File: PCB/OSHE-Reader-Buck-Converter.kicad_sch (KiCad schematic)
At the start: 18 parts, among them U3 TPS5432DDA

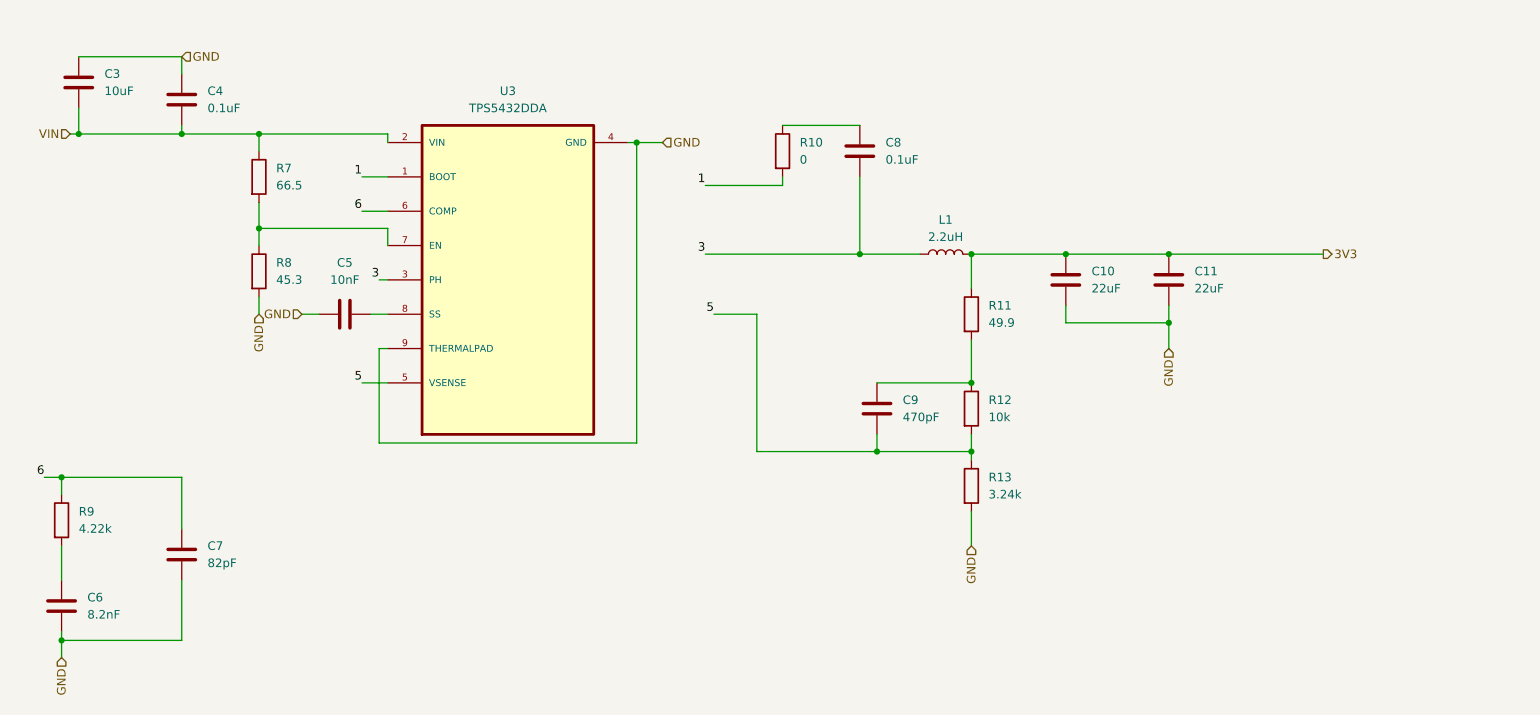
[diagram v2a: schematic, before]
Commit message: Footprints added
All footprints added (problem with J1 for some reason) ((pads of the display driver))
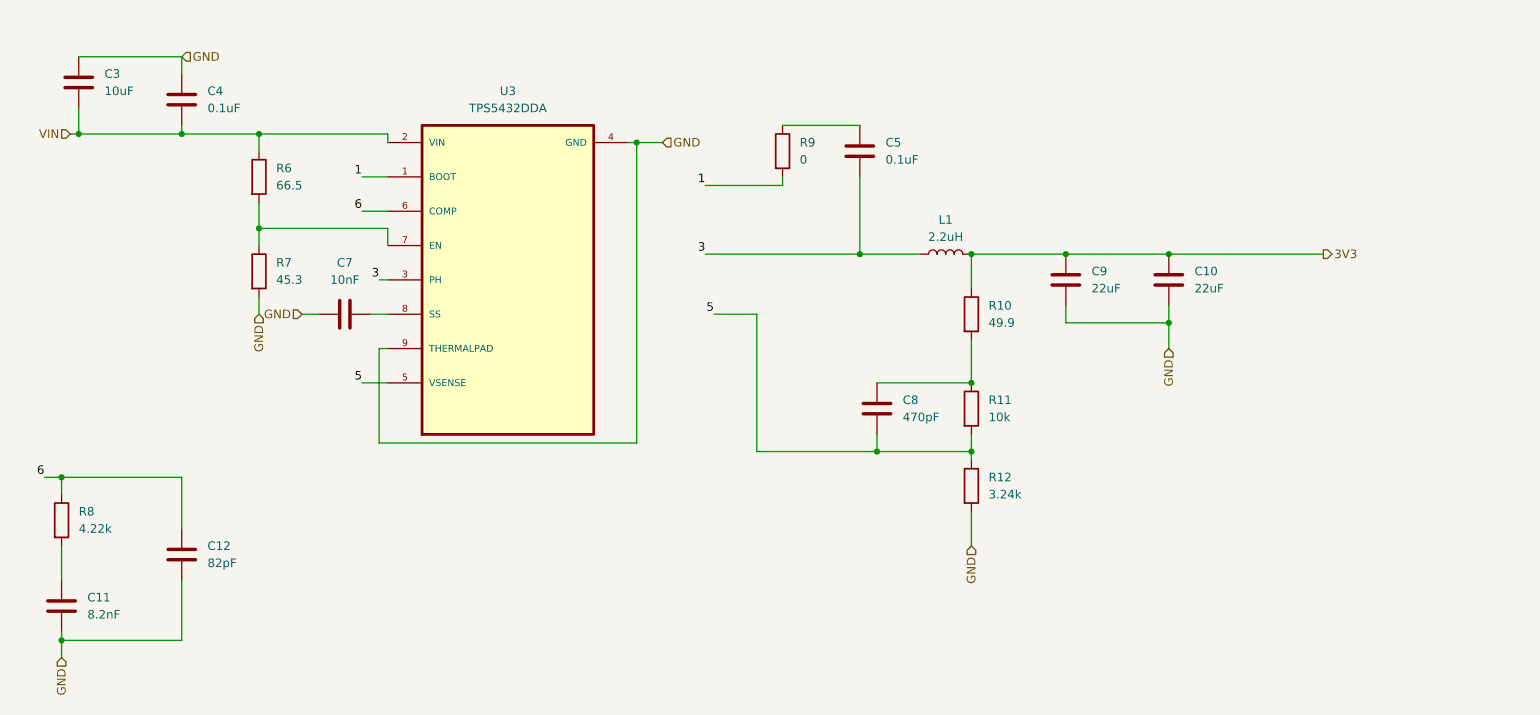
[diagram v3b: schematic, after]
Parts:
- C10: renamed from C11; footprint (none) -> Capacitor_SMD:C_1206_3216Metric
- C11: renamed from C6; footprint (none) -> Capacitor_SMD:C_1206_3216Metric
- C12: renamed from C7; footprint (none) -> Capacitor_SMD:C_1206_3216Metric
- C3, C4: footprint (none) -> Capacitor_SMD:C_1206_3216Metric
- C5: renamed from C8; footprint (none) -> Capacitor_SMD:C_1206_3216Metric
- C7: renamed from C5; footprint (none) -> Capacitor_SMD:C_1206_3216Metric
- C8: renamed from C9; footprint (none) -> Capacitor_SMD:C_1206_3216Metric
- C9: renamed from C10; footprint (none) -> Capacitor_SMD:C_1206_3216Metric
- L1: footprint (none) -> Inductor_SMD:L_1206_3216Metric
- R10: renamed from R11; footprint (none) -> Resistor_SMD:R_1206_3216Metric
- R11: renamed from R12; footprint (none) -> Resistor_SMD:R_1206_3216Metric
- R12: renamed from R13; footprint (none) -> Resistor_SMD:R_1206_3216Metric
- R6: renamed from R7; footprint (none) -> Resistor_SMD:R_1206_3216Metric
- R7: renamed from R8; footprint (none) -> Resistor_SMD:R_1206_3216Metric
- R8: renamed from R9; footprint (none) -> Resistor_SMD:R_1206_3216Metric
- R9: renamed from R10; footprint (none) -> Resistor_SMD:R_1206_3216Metric
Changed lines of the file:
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@@
 		(dnp no)
 		(fields_autoplaced yes)
-		(property "Reference" "R9"
+		(property "Reference" "R8"
 			(at 31.75 82.5499 0)
 			(effects
@@
 			)
 		)
-		(property "Footprint" ""
+		(property "Footprint" "Resistor_SMD:R_1206_3216Metric"
 			(at 27.432 83.82 90)
 			(effects
@@
 				)
 			)
+			(project "OSHE-Reader-Buck-Converter"
+				(path "/d789ce52-9213-4e29-8b23-52a67eafd209"
+					(reference "R8")
+					(unit 1)
+				)
+			)
 		)
 	)
@@
 		(dnp no)
 		(fields_autoplaced yes)
-		(property "Reference" "C11"
+		(property "Reference" "C10"
 			(at 196.85 46.9899 0)
 			(effects
@@
 			)
 		)
-		(property "Footprint" ""
+		(property "Footprint" "Capacitor_SMD:C_1206_3216Metric"
 			(at 192.0748 44.45 0)
 			(effects
@@
 				)
 			)
+			(project "OSHE-Reader-Buck-Converter"
+				(path "/d789ce52-9213-4e29-8b23-52a67eafd209"
+					(reference "C10")
+					(unit 1)
+				)
+			)
 		)
 	)
@@
 		(dnp no)
 		(fields_autoplaced yes)
-		(property "Reference" "C10"
+		(property "Reference" "C9"
 			(at 181.61 46.9899 0)
 			(effects
@@
 			)
 		)
-		(property "Footprint" ""
+		(property "Footprint" "Capacitor_SMD:C_1206_3216Metric"
 			(at 176.8348 44.45 0)
 			(effects
@@
 				)
 			)
+			(project "OSHE-Reader-Buck-Converter"
+				(path "/d789ce52-9213-4e29-8b23-52a67eafd209"
+					(reference "C9")
+					(unit 1)
+				)
+			)
 		)
 	)
@@
 		(dnp no)
 		(fields_autoplaced yes)
-		(property "Reference" "R10"
+		(property "Reference" "R9"
 			(at 138.43 27.9399 0)
 			(effects
@@
 			)
 		)
-		(property "Footprint" ""
+		(property "Footprint" "Resistor_SMD:R_1206_3216Metric"
 			(at 134.112 29.21 90)
 			(effects
@@
 				)
 			)
+			(project "OSHE-Reader-Buck-Converter"
+				(path "/d789ce52-9213-4e29-8b23-52a67eafd209"
+					(reference "R9")
+					(unit 1)
+				)
+			)
 		)
 	)
@@
 		(dnp no)
 		(fields_autoplaced yes)
-		(property "Reference" "C7"
+		(property "Reference" "C12"
 			(at 50.8 87.6299 0)
 			(effects
@@
 			)
 		)
-		(property "Footprint" ""
+		(property "Footprint" "Capacitor_SMD:C_1206_3216Metric"
 			(at 47.9552 92.71 0)
 			(effects
@@
 				)
 			)
+			(project "OSHE-Reader-Buck-Converter"
+				(path "/d789ce52-9213-4e29-8b23-52a67eafd209"
+					(reference "C12")
+					(unit 1)
+				)
+			)
 		)
 	)
@@
 		(dnp no)
 		(fields_autoplaced yes)
-		(property "Reference" "R13"
+		(property "Reference" "R12"
 			(at 166.37 77.4699 0)
 			(effects
@@
 			)
 		)
-		(property "Footprint" ""
+		(property "Footprint" "Resistor_SMD:R_1206_3216Metric"
 			(at 162.052 78.74 90)
 			(effects
@@
 				)
 			)
+			(project "OSHE-Reader-Buck-Converter"
+				(path "/d789ce52-9213-4e29-8b23-52a67eafd209"
+					(reference "R12")
+					(unit 1)
+				)
+			)
 		)
 	)
@@
 		(dnp no)
 		(fields_autoplaced yes)
-		(property "Reference" "R7"
+		(property "Reference" "R6"
 			(at 60.96 31.7499 0)
 			(effects
@@
 			)
 		)
-		(property "Footprint" ""
+		(property "Footprint" "Resistor_SMD:R_1206_3216Metric"
 			(at 56.642 33.02 90)
 			(effects
@@
 				)
 			)
+			(project "OSHE-Reader-Buck-Converter"
+				(path "/d789ce52-9213-4e29-8b23-52a67eafd209"
+					(reference "R6")
+					(unit 1)
+				)
+			)
 		)
 	)
@@
 		(dnp no)
 		(fields_autoplaced yes)
-		(property "Reference" "R8"
+		(property "Reference" "R7"
 			(at 60.96 45.7199 0)
 			(effects
@@
 			)
 		)
-		(property "Footprint" ""
+		(property "Footprint" "Resistor_SMD:R_1206_3216Metric"
 			(at 56.642 46.99 90)
 			(effects
@@
 				)
 			)
+			(project "OSHE-Reader-Buck-Converter"
+				(path "/d789ce52-9213-4e29-8b23-52a67eafd209"
+					(reference "R7")
+					(unit 1)
+				)
+			)
 		)
 	)
@@
 		(dnp no)
 		(fields_autoplaced yes)
-		(property "Reference" "C6"
+		(property "Reference" "C11"
 			(at 33.02 95.2499 0)
 			(effects
@@
 			)
 		)
-		(property "Footprint" ""
+		(property "Footprint" "Capacitor_SMD:C_1206_3216Metric"
 			(at 30.1752 100.33 0)
 			(effects
@@
 				)
 			)
+			(project "OSHE-Reader-Buck-Converter"
+				(path "/d789ce52-9213-4e29-8b23-52a67eafd209"
+					(reference "C11")
+					(unit 1)
+				)
+			)
 		)
 	)
@@
 		(dnp no)
 		(fields_autoplaced yes)
-		(property "Reference" "R12"
+		(property "Reference" "R11"
 			(at 166.37 66.0399 0)
 			(effects
@@
 			)
 		)
-		(property "Footprint" ""
+		(property "Footprint" "Resistor_SMD:R_1206_3216Metric"
 			(at 162.052 67.31 90)
 			(effects
@@
 				)
 			)
+			(project "OSHE-Reader-Buck-Converter"
+				(path "/d789ce52-9213-4e29-8b23-52a67eafd209"
+					(reference "R11")
+					(unit 1)
+				)
+			)
 		)
 	)
@@
 		(dnp no)
 		(fields_autoplaced yes)
-		(property "Reference" "R11"
+		(property "Reference" "R10"
 			(at 166.37 52.0699 0)
 			(effects
@@
 			)
 		)
-		(property "Footprint" ""
+		(property "Footprint" "Resistor_SMD:R_1206_3216Metric"
 			(at 162.052 53.34 90)
 			(effects
@@
 				)
 			)
+			(project "OSHE-Reader-Buck-Converter"
+				(path "/d789ce52-9213-4e29-8b23-52a67eafd209"
+					(reference "R10")
+					(unit 1)
+				)
+			)
 		)
 	)
@@
 			)
 		)
-		(property "Footprint" ""
+		(property "Footprint" "Capacitor_SMD:C_1206_3216Metric"
 			(at 47.9552 25.4 0)
 			(effects
@@
 				)
 			)
+			(project "OSHE-Reader-Buck-Converter"
+				(path "/d789ce52-9213-4e29-8b23-52a67eafd209"
+					(reference "C4")
+					(unit 1)
+				)
+			)
 		)
 	)
@@
 			)
 		)
-		(property "Footprint" ""
+		(property "Footprint" "Inductor_SMD:L_1206_3216Metric"
 			(at 160.02 44.45 0)
 			(effects
@@
 				)
 			)
+			(project "OSHE-Reader-Buck-Converter"
+				(path "/d789ce52-9213-4e29-8b23-52a67eafd209"
+					(reference "L1")
+					(unit 1)
+				)
+			)
 		)
 	)
@@
 		(dnp no)
 		(fields_autoplaced yes)
-		(property "Reference" "C5"
+		(property "Reference" "C7"
 			(at 71.12 45.72 90)
 			(effects
@@
 			)
 		)
-		(property "Footprint" ""
+		(property "Footprint" "Capacitor_SMD:C_1206_3216Metric"
 			(at 74.93 52.3748 0)
 			(effects
@@
 				)
 			)
+			(project "OSHE-Reader-Buck-Converter"
+				(path "/d789ce52-9213-4e29-8b23-52a67eafd209"
+					(reference "C7")
+					(unit 1)
+				)
+			)
 		)
 	)
@@
 			)
 		)
-		(property "Footprint" ""
+		(property "Footprint" "Capacitor_SMD:C_1206_3216Metric"
 			(at 32.7152 22.86 0)
 			(effects
@@
 				)
 			)
+			(project "OSHE-Reader-Buck-Converter"
+				(path "/d789ce52-9213-4e29-8b23-52a67eafd209"
+					(reference "C3")
+					(unit 1)
+				)
+			)
 		)
 	)
@@
 		(dnp no)
 		(fields_autoplaced yes)
-		(property "Reference" "C8"
+		(property "Reference" "C5"
 			(at 151.13 27.9399 0)
 			(effects
@@
 			)
 		)
-		(property "Footprint" ""
+		(property "Footprint" "Capacitor_SMD:C_1206_3216Metric"
 			(at 146.3548 25.4 0)
 			(effects
@@
 				)
 			)
+			(project "OSHE-Reader-Buck-Converter"
+				(path "/d789ce52-9213-4e29-8b23-52a67eafd209"
+					(reference "C5")
+					(unit 1)
+				)
+			)
 		)
 	)
@@
 		(dnp no)
 		(fields_autoplaced yes)
-		(property "Reference" "C9"
+		(property "Reference" "C8"
 			(at 153.67 66.0399 0)
 			(effects
@@
 			)
 		)
-		(property "Footprint" ""
+		(property "Footprint" "Capacitor_SMD:C_1206_3216Metric"
 			(at 148.8948 63.5 0)
 			(effects
@@
 				)
 			)
+			(project "OSHE-Reader-Buck-Converter"
+				(path "/d789ce52-9213-4e29-8b23-52a67eafd209"
+					(reference "C8")
+					(unit 1)
+				)
+			)
 		)
 	)
@@
 				)
 			)
-		)
-	)
+			(project "OSHE-Reader-Buck-Converter"
+				(path "/d789ce52-9213-4e29-8b23-52a67eafd209"
+					(reference "U3")
+					(unit 1)
+				)
+			)
+		)
+	)
+	(sheet_instances
+		(path "/"
+			(page "1")
+		)
+	)
+	(embedded_fonts no)
 )

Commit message: Did a bunch of work with final preparations of the schematic for pcb routing
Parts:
- renumbered C9 to C10, C10 to C11, C7 to C5, C11 to C6, C12 to C7, C5 to C8, C8 to C9, R9 to R10, R10 to R11, R11 to R12, R12 to R13, R6 to R7, R7 to R8, R8 to R9
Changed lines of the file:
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@@
 		(dnp no)
 		(fields_autoplaced yes)
-		(property "Reference" "R8"
+		(property "Reference" "R9"
 			(at 31.75 82.5499 0)
 			(effects
@@
 		(dnp no)
 		(fields_autoplaced yes)
-		(property "Reference" "C10"
+		(property "Reference" "C11"
 			(at 196.85 46.9899 0)
 			(effects
@@
 		(dnp no)
 		(fields_autoplaced yes)
-		(property "Reference" "C9"
+		(property "Reference" "C10"
 			(at 181.61 46.9899 0)
 			(effects
@@
 		(dnp no)
 		(fields_autoplaced yes)
-		(property "Reference" "R9"
+		(property "Reference" "R10"
 			(at 138.43 27.9399 0)
 			(effects
@@
 		(dnp no)
 		(fields_autoplaced yes)
-		(property "Reference" "C12"
+		(property "Reference" "C7"
 			(at 50.8 87.6299 0)
 			(effects
@@
 		(dnp no)
 		(fields_autoplaced yes)
-		(property "Reference" "R12"
+		(property "Reference" "R13"
 			(at 166.37 77.4699 0)
 			(effects
@@
 		(dnp no)
 		(fields_autoplaced yes)
-		(property "Reference" "R6"
+		(property "Reference" "R7"
 			(at 60.96 31.7499 0)
 			(effects
@@
 		(dnp no)
 		(fields_autoplaced yes)
-		(property "Reference" "R7"
+		(property "Reference" "R8"
 			(at 60.96 45.7199 0)
 			(effects
@@
 		(dnp no)
 		(fields_autoplaced yes)
-		(property "Reference" "C11"
+		(property "Reference" "C6"
 			(at 33.02 95.2499 0)
 			(effects
@@
 		(dnp no)
 		(fields_autoplaced yes)
-		(property "Reference" "R11"
+		(property "Reference" "R12"
 			(at 166.37 66.0399 0)
 			(effects
@@
 		(dnp no)
 		(fields_autoplaced yes)
-		(property "Reference" "R10"
+		(property "Reference" "R11"
 			(at 166.37 52.0699 0)
 			(effects
@@
 		(dnp no)
 		(fields_autoplaced yes)
-		(property "Reference" "C7"
+		(property "Reference" "C5"
 			(at 71.12 45.72 90)
 			(effects
@@
 		(dnp no)
 		(fields_autoplaced yes)
-		(property "Reference" "C5"
+		(property "Reference" "C8"
 			(at 151.13 27.9399 0)
 			(effects
@@
 		(dnp no)
 		(fields_autoplaced yes)
-		(property "Reference" "C8"
+		(property "Reference" "C9"
 			(at 153.67 66.0399 0)
 			(effects

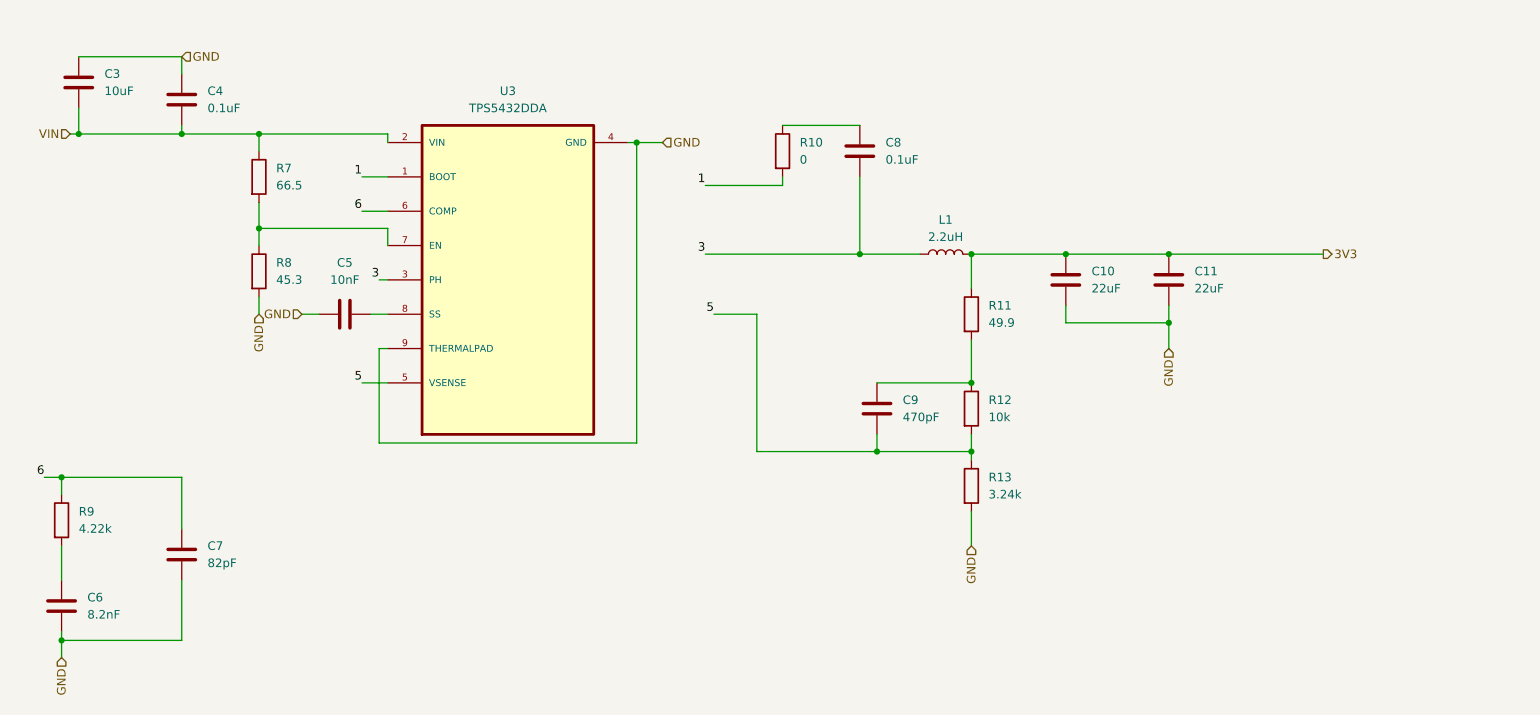
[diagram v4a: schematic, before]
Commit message: Re-did buck converter schematic sheet to more closely resemble TI's datasheet, implemented buck converter on PCB following TI's datasheet layout example
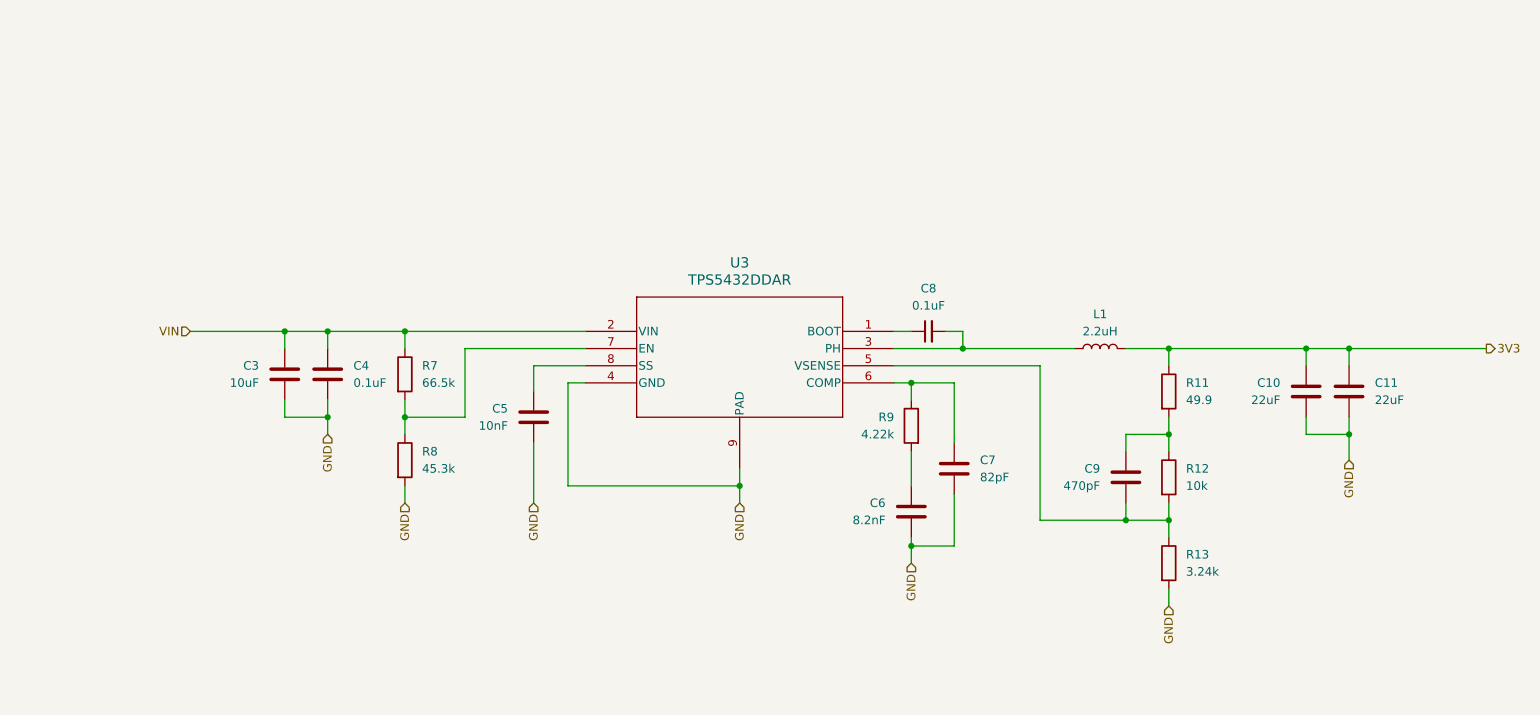
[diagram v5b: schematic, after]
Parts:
- removed C8: 0.1uF, Capacitor_SMD:C_1206_3216Metric, symbol Device:C
- removed R10: 0, Resistor_SMD:R_1206_3216Metric, symbol Device:R
- removed U3: TPS5432DDA, TPS5432DDAR:DDA_R-PDSO-G8_TEX, symbol TPS5432DDA:TPS5432DDA
- added C8: 0.1uF, Capacitor_SMD:C_1206_3216Metric, symbol Device:C_Small
- added U3: TPS5432DDAR, DDA_R-PDSO-G8_TEX, symbol TPS5432DDAR:TPS5432DDAR
- R7: value 66.5 -> 66.5k
- R8: value 45.3 -> 45.3k
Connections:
- net GND: now also C3.2, C4.2, C5.2, U3.4 (GND), U3.9 (PAD); no longer C3.1, C4.1, C5.1
- net VIN: now also C3.1, C4.1, U3.2 (VIN); no longer C3.2, C4.2
- net at R7.2, R8.1: now also U3.7 (EN)
- net 3: no longer names the net of L1.1
- net 3: now also C8.2, U3.3 (PH)
- net 5: no longer names the net of C9.1, R12.2, R13.1
- net 5: now also U3.5 (VSENSE)
- net 6: no longer names the net of C7.1, R9.1
- net 6: now also U3.6 (COMP)
- new net: C8.1, U3.1 (BOOT)
- new net: C5.1, U3.8 (SS)
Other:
- moved on the sheet: C11, C3, C4, C6, C7, L1, R12, R13, R9
